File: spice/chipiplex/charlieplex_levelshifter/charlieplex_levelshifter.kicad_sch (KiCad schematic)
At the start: 42 parts, among them Q1 NPN, Q2 PNP, Q3 PNP, Q4 NPN, Q5 PNP, Q6 NPN, Q7 PNP, Q8 NPN

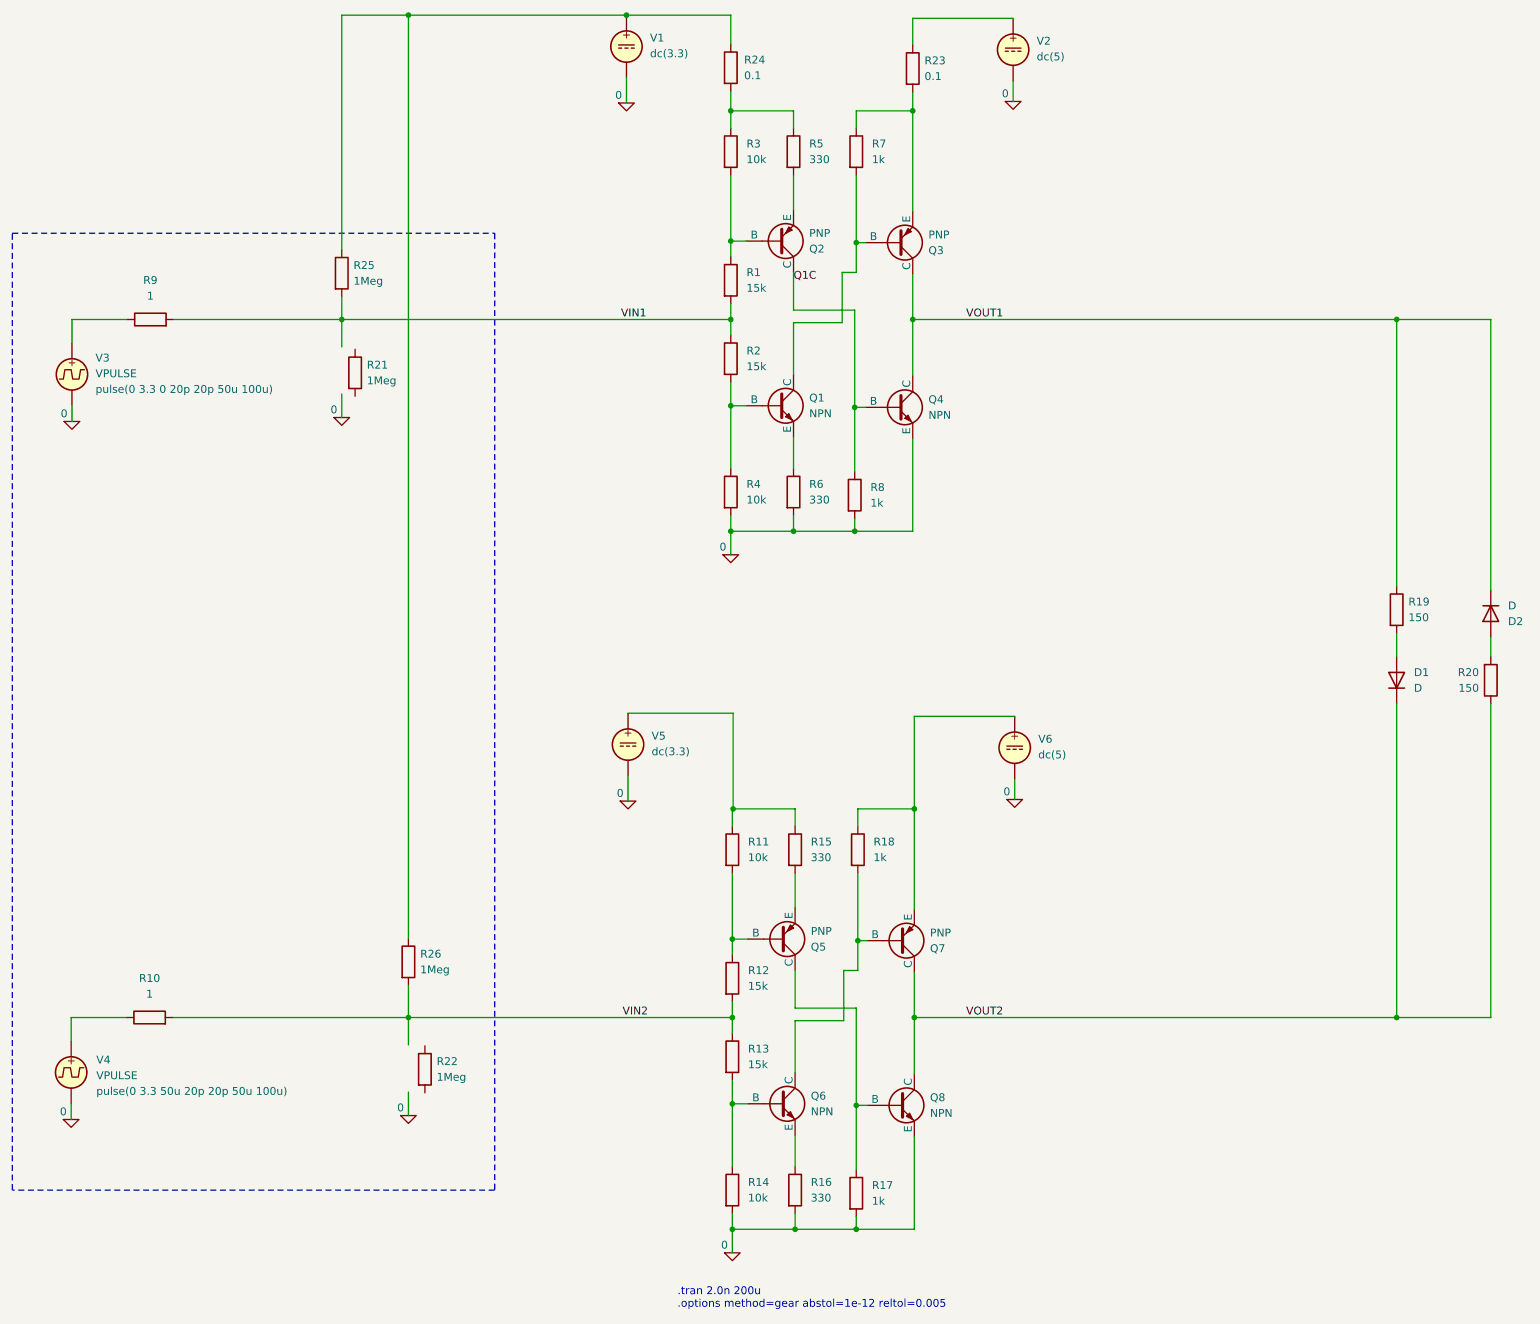
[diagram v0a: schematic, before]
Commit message: Worked on spice models.
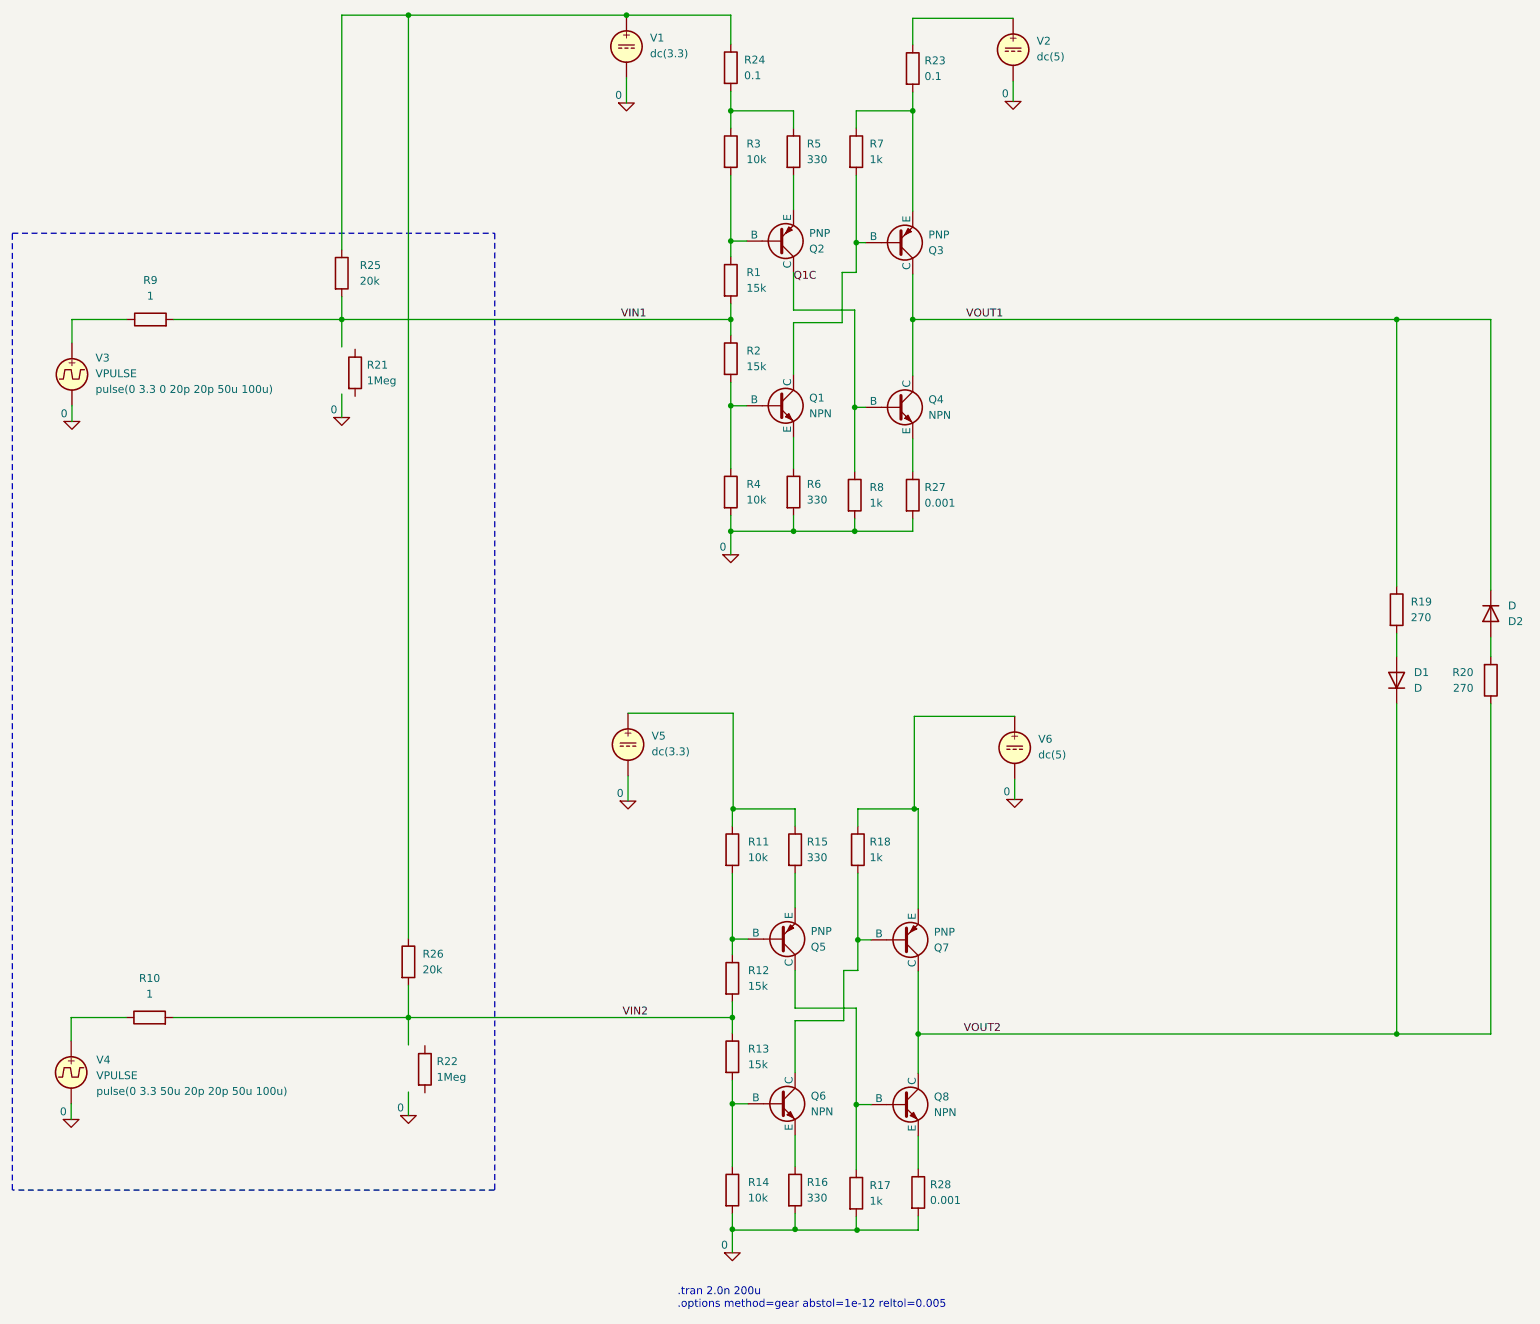
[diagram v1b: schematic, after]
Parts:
- added R27, R28: 0.001, symbol Device:R
- R19, R20: value 150 -> 270
- R25, R26: value 1Meg -> 20k
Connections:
- net 0: now also R27.2, R28.2; no longer Q4.3 (E), Q8.3 (E)
- new net: Q4.3 (E), R27.1
- new net: Q8.3 (E), R28.1
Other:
- moved on the sheet: Q7, Q8
